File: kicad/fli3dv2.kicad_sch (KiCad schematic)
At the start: 20 parts, among them J1 BAT connector, J2 Conn_Serial, J3 Separation Detect, J4 Parachute Release, J5 Conn_Power, J7 Conn_IO, K1 HFD4_4.5-SR, SW1 PWR jumper, SW2 SW_DIP, U3 ESP32-CAM, U8 esp32-wemos-d1-mini

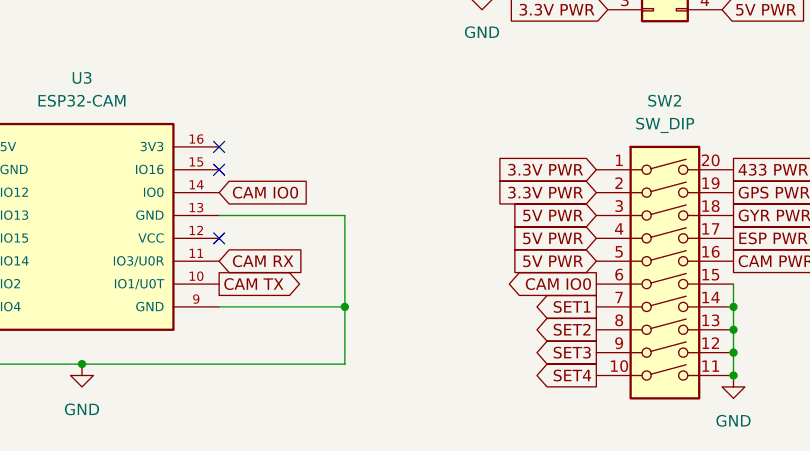
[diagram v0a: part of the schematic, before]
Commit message: PCB v0.4.1: set GY912 on 3.3V and decoupled ESP32CAM GND/R
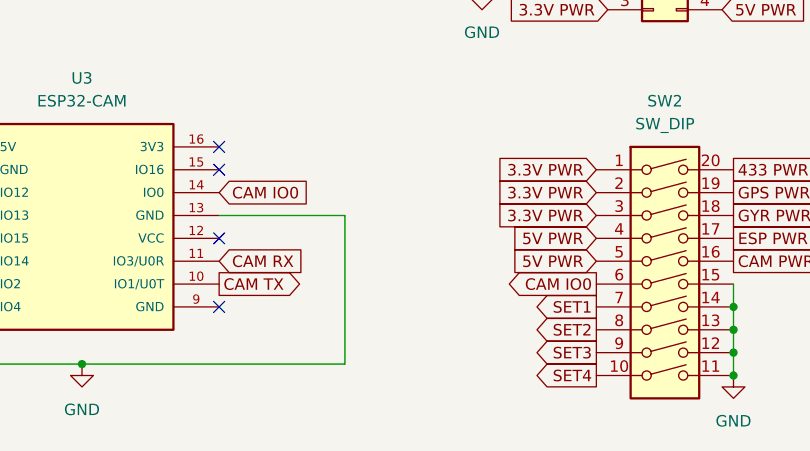
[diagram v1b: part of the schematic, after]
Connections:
- net 3.3V PWR: now also SW2.3
- net 5V PWR: no longer SW2.3
- net GND: no longer U3.9 (GND)
- no-connect marks 25 -> 26
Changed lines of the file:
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@@
-	)
-	(junction
-		(at 77.47 147.32)
-		(diameter 0)
-		(color 0 0 0 0)
 	)
 	(junction
@@
 	)
 	(no_connect
+		(at 63.5 147.32)
+	)
+	(no_connect
 		(at 265.43 80.01)
 	)
@@
 	(wire
 		(pts
-			(xy 77.47 137.16) (xy 77.47 147.32)
-		)
-		(stroke
-			(width 0)
-			(type default)
-		)
-	)
-	(wire
-		(pts
 			(xy 63.5 137.16) (xy 77.47 137.16)
 		)
@@
 	(wire
 		(pts
-			(xy 63.5 147.32) (xy 77.47 147.32)
-		)
-		(stroke
-			(width 0)
-			(type default)
-		)
-	)
-	(wire
-		(pts
 			(xy 119.38 86.36) (xy 128.27 86.36)
 		)
@@
 	(wire
 		(pts
-			(xy 77.47 153.67) (xy 77.47 147.32)
+			(xy 77.47 137.16) (xy 77.47 153.67)
 		)
 		(stroke
@@
 		)
 	)
-	(global_label "5V PWR"
+	(global_label "3.3V PWR"
 		(shape input)
 		(at 105.41 137.16 180)
@@
 		)
 		(property "Intersheetrefs" "${INTERSHEET_REFS}"
-			(at 95.1677 137.16 0)
-			(effects
-				(font
+			(at 93.3534 137.16 0)
+			(effects
+				(font
